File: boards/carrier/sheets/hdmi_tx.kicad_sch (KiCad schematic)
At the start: 21 parts

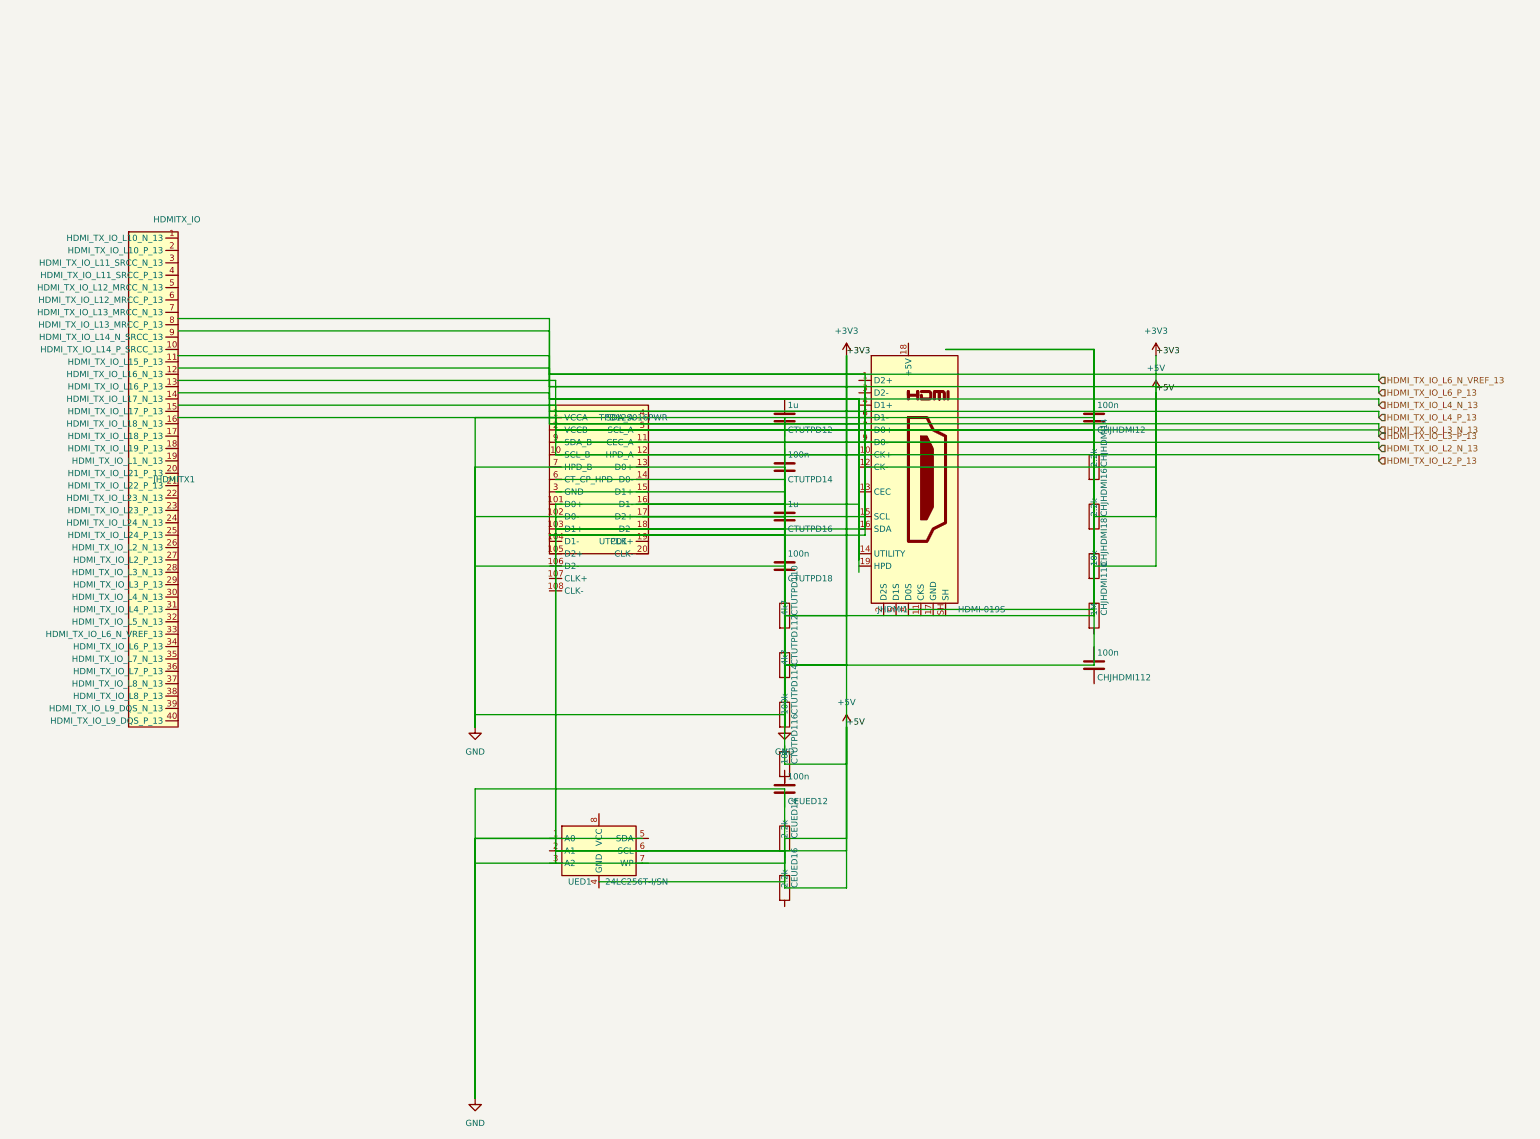
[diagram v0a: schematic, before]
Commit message: hdmi: use Connector_Generic:Conn_01x19 (Connector lib not auto-discovered)
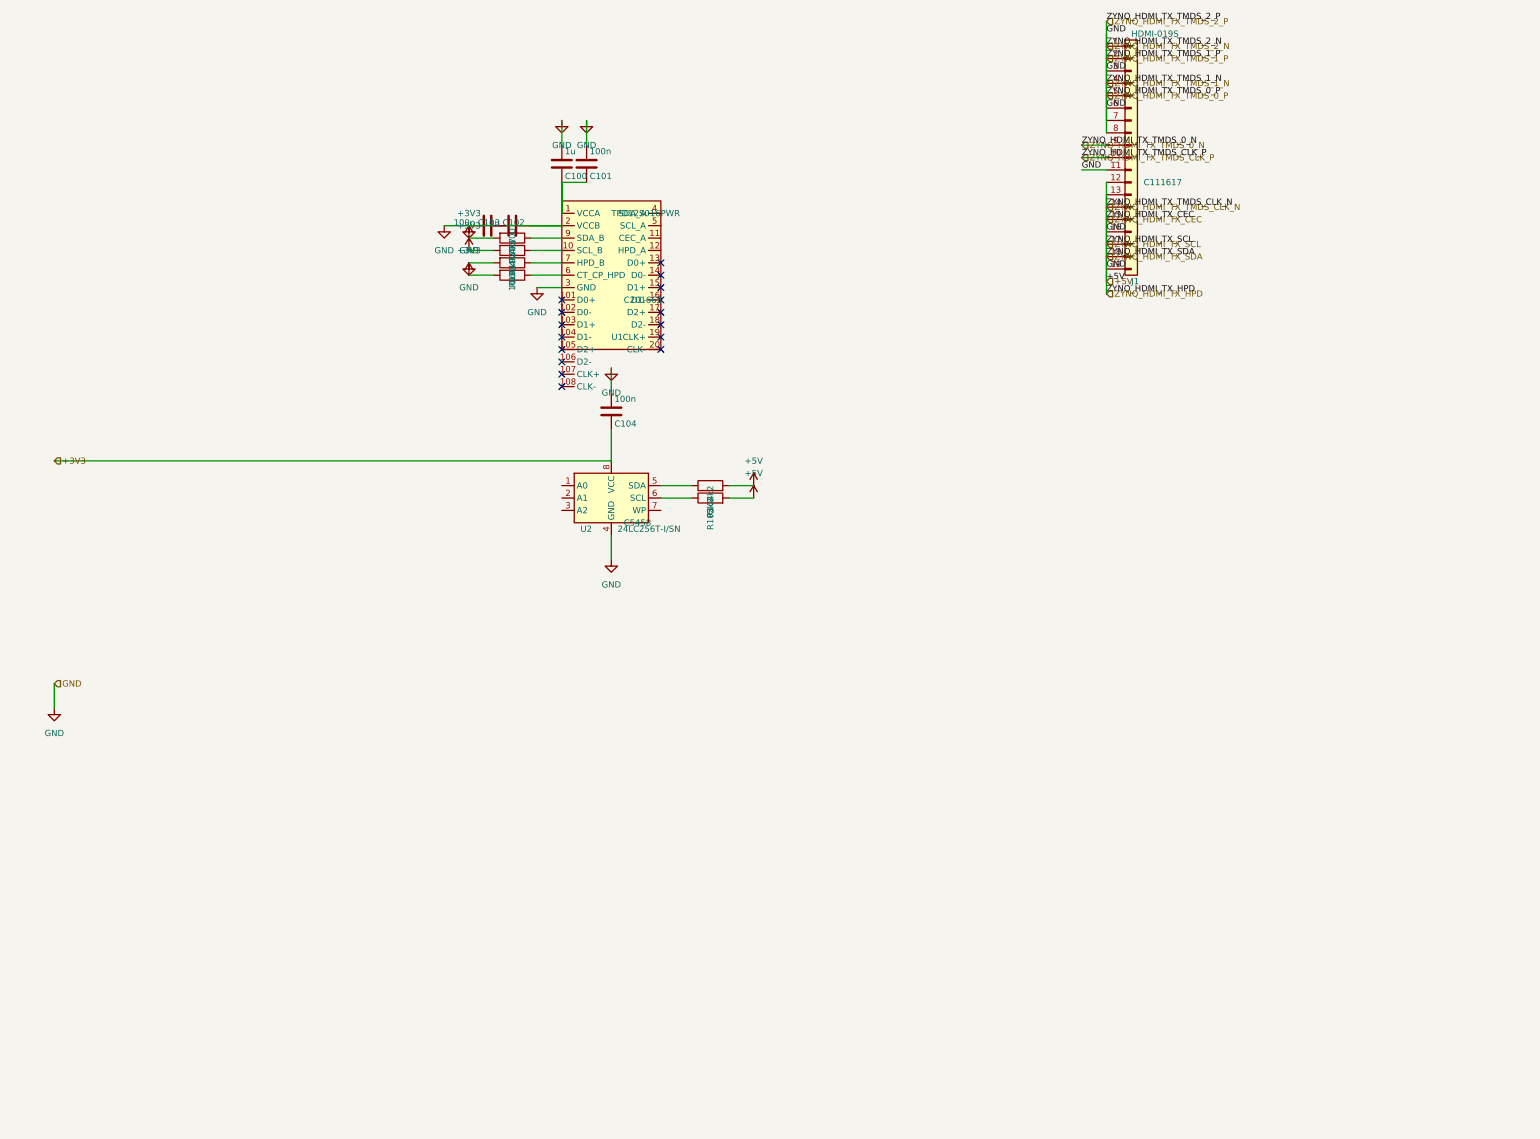
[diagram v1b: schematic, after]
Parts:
- removed CEUED12, CHJHDMI112, CHJHDMI12, CTUTPD14, CTUTPD18: 100n, Capacitor_SMD:C_0402_1005Metric, symbol Device:C
- removed CEUED14, CEUED16, CHJHDMI14, CHJHDMI16: 2.2k, Resistor_SMD:R_0402_1005Metric, symbol Device:R
- removed CHJHDMI110: 1M, Resistor_SMD:R_0402_1005Metric, symbol Device:R
- removed CHJHDMI18, CTUTPD116: 10k, Resistor_SMD:R_0402_1005Metric, symbol Device:R
- removed CTUTPD110, CTUTPD112: 4k7, Resistor_SMD:R_0402_1005Metric, symbol Device:R
- removed CTUTPD114: 100k, Resistor_SMD:R_0402_1005Metric, symbol Device:R
- removed CTUTPD12, CTUTPD16: 1u, Capacitor_SMD:C_0402_1005Metric, symbol Device:C
- removed JHDMI1: HDMI-019S, Connector_HDMI:HDMI_A_SOFNG_HDMI-019S, symbol Connector:HDMI_A
- removed JHDMITX1: HDMITX_IO, symbol HDMITX_IO:HDMITX_IO
- removed UED1: 24LC256T-I/SN, Package_SO:SOIC-8_3.9x4.9mm_P1.27mm, symbol Memory_EEPROM:24LC256
- removed UTPD1: TPD12S016PWR, Package_SO:TSSOP-24_4.4x7.8mm_P0.65mm, symbol carrier:TPD12S016PWR
- added C100, C102: 1u, Capacitor_SMD:C_0402_1005Metric, symbol Device:C
- added C101, C103, C104: 100n, Capacitor_SMD:C_0402_1005Metric, symbol Device:C
- added J1: HDMI-019S, Connector_HDMI:HDMI_A_SOFNG_HDMI-019S, symbol Connector_Generic:Conn_01x19
- added R100, R101: 4k7, Resistor_SMD:R_0402_1005Metric, symbol Device:R
- added R102: 100k, Resistor_SMD:R_0402_1005Metric, symbol Device:R
- added R103: 10k, Resistor_SMD:R_0402_1005Metric, symbol Device:R
- added R104, R105: 2k2, Resistor_SMD:R_0402_1005Metric, symbol Device:R
- added U1: TPD12S016PWR, Package_SO:TSSOP-24_4.4x7.8mm_P0.65mm, symbol zynq_eda:TPD12S016PWR
- added U2: 24LC256T-I/SN, Package_SO:SOIC-8_3.9x4.9mm_P1.27mm, symbol Memory_EEPROM:24LC256
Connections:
- net +3V3: now also C104.2, R100.2, R101.2, R103.2, U2.8 (VCC)
- new net: R104.1, U2.5 (SDA)
- new net: C102.1, C103.1, U1.2 (VCCB)
- new net: C100.2, C101.2, U1.1 (VCCA)
- new net: R101.1, U1.10 (SCL_B)
- new net: R103.1, U1.6 (CT_CP_HPD)
- new net: R102.1, U1.7 (HPD_B)
- new net: R100.1, U1.9 (SDA_B)
- new net: R105.1, U2.6 (SCL)
- new net +5V: C100.1, C101.1, C102.2, C103.2, C104.1, J1.1 (Pin_1), J1.11 (Pin_11), J1.12 (Pin_12), J1.13 (Pin_13), J1.14 (Pin_14), J1.15 (Pin_15), J1.16 (Pin_16), J1.17 (Pin_17), J1.18 (Pin_18), J1.19 (Pin_19), J1.2 (Pin_2), J1.3 (Pin_3), J1.4 (Pin_4), J1.5 (Pin_5), J1.6 (Pin_6), J1.7 (Pin_7), J1.8 (Pin_8), R102.2, R104.2, R105.2, U1.3 (GND), U2.4 (GND)
- new net ZYNQ_HDMI_TX_TMDS_0_N: J1.9 (Pin_9)
- new net ZYNQ_HDMI_TX_TMDS_CLK_P: J1.10 (Pin_10)
- no-connect marks 0 -> 16
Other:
- title: HDMI TX (TPD12S016 + HDMI + EDID) -> HDMI Transmitter (Zynq → TPD12S016 → HDMI-A)
